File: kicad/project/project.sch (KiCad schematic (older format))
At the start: 47 parts, among them J1 SWD, J3 Voltmeter, Q1 Si2319CDS, Q2 2N7002, U1 ADS1015, U2 AP7380, U3 STM32L031F4Px, U4 VN7003ALH

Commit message: Tuning
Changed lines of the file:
@@
 	1400 7275 1400 7125
-Wire Wire Line
-	4300 3925 4550 3925
 Wire Wire Line
 	6000 3075 6000 3150
@@
 	0    -1   -1   0
 $EndComp
-Connection ~ 4550 3925
-Wire Wire Line
-	4550 3925 6650 3925
 Wire Wire Line
 	6850 4225 6850 4075
@@
 	9925 2975 9825 2975
 Connection ~ 9825 2975
+Wire Wire Line
+	4550 3925 6650 3925
 $EndSCHEMATC

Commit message: VN7004CLHTR
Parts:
- removed BT1: Battery_Meter, theapi:TerminalBlock_Meter, symbol theapi_Battery:Battery_Meter
- removed C2: 0.1UF, Capacitor_SMD:C_0603_1608Metric_Pad1.05x0.95mm_HandSolder, symbol project-rescue:C-stm32l053c-rescue
- removed D5: D_Schottky, Diode_THT:D_DO-201AD_P12.70mm_Horizontal, symbol Device:D_Schottky
- removed H3, H4: MountingHole_Pad, MountingHole:MountingHole_3.2mm_M3_Pad, symbol Mechanical:MountingHole_Pad
- removed J3: Voltmeter, theapi:Voltmeter_Header_1x03, symbol Connector:Conn_01x03_Male
- removed R4, R5, R6: 10K, Resistor_SMD:R_0603_1608Metric_Pad1.05x0.95mm_HandSolder, symbol project-rescue:R-stm32l053c-rescue
- removed TP1: TestPoint, TestPoint:TestPoint_Pad_D1.0mm, symbol Connector:TestPoint
- removed U1: ADS1015, theapi:TSSOP-10_3x3mm_P0.5mm, symbol project-rescue:ADS1015-adc
- added BT1: Battery, TerminalBlock:TerminalBlock_bornier-2_P5.08mm, symbol Device:Battery
- C9: value 1uF -> 220pF
- U4: value VN7003ALH -> VN7004CLHTR
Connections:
- net GND: now also BT1.2 (-)
- net OUT: now also Q1.2 (S), BT1.1 (+)
- net at Q1.3 (D), R14.1: now also R10.1
- net at Q1.1 (G), Q2.3 (D): now also R10.2; no longer R10.1
- removed net DIODE: Q1.2 (S), R10.2
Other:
- note removed: "Optional External ADC"
- moved on the sheet: R10

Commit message: VN7004CLHTR
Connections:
- net ADC_RDY: no longer names the net of U3.13 (PA7)
- net SCL: no longer names the net of U3.17 (PA9)
- net SDA: no longer names the net of U3.18 (PA10)
- no-connect marks 1 -> 4
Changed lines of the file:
@@
 	1    0    0    -1
 $EndComp
-Text GLabel 4550 4625 2    50   Input ~ 0
-SCL
-Text GLabel 4550 4725 2    50   Input ~ 0
-SDA
 Text GLabel 3550 4925 0    50   Input ~ 0
 CURRENT_SENSE
@@
 Text GLabel 6150 1850 2    50   Input ~ 0
 UART_TX
-Text GLabel 4550 4525 2    60   Input ~ 0
-ADC_RDY
 Wire Wire Line
 	6000 3075 6000 3150
@@
 Wire Wire Line
 	10225 2675 10225 4475
+NoConn ~ 4550 4625
+NoConn ~ 4550 4525
+NoConn ~ 4550 4725
 $EndSCHEMATC

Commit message: New layout
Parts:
- removed D4: LED, LED_SMD:LED_0805_2012Metric_Pad1.15x1.40mm_HandSolder, symbol Device:LED
- removed H2: MountingHole_Pad, MountingHole:MountingHole_3.2mm_M3_Pad, symbol Mechanical:MountingHole_Pad
- removed R17: 10K, Resistor_SMD:R_0603_1608Metric_Pad1.05x0.95mm_HandSolder, symbol Device:R
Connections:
- net OUT: now also R10.1
- net at Q1.3 (D), R14.1: no longer R10.1
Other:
- moved on the sheet: R10
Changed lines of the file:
@@
 	8625 3500 9125 3500
-$Comp
-L Device:R R17
-U 1 1 5C7C0432
-P 9150 4850
-F 0 "R17" H 9220 4896 50  0000 L CNN
-F 1 "10K" H 9220 4805 50  0000 L CNN
-F 2 "Resistor_SMD:R_0603_1608Metric_Pad1.05x0.95mm_HandSolder" V 9080 4850 50  0001 C CNN
-F 3 "~" H 9150 4850 50  0001 C CNN
-	1    9150 4850
-	1    0    0    -1
-$EndComp
-$Comp
-L Device:LED D4
-U 1 1 5C7C051B
-P 9150 5300
-F 0 "D4" V 9188 5183 50  0000 R CNN
-F 1 "LED" V 9097 5183 50  0000 R CNN
-F 2 "LED_SMD:LED_0805_2012Metric_Pad1.15x1.40mm_HandSolder" H 9150 5300 50  0001 C CNN
-F 3 "~" H 9150 5300 50  0001 C CNN
-	1    9150 5300
-	0    -1   -1   0
-$EndComp
-$Comp
-L power:GND #PWR032
-U 1 1 5C7C05D8
-P 9150 5450
-F 0 "#PWR032" H 9150 5200 50  0001 C CNN
-F 1 "GND" H 9155 5277 50  0000 C CNN
-F 2 "" H 9150 5450 50  0001 C CNN
-F 3 "" H 9150 5450 50  0001 C CNN
-	1    9150 5450
-	1    0    0    -1
-$EndComp
-Wire Wire Line
-	9150 5150 9150 5000
 $Comp
 L Device:LED D1
@@
 	8900 4675 8900 4575
 Connection ~ 8900 4575
-Wire Wire Line
-	8900 4475 9150 4475
 Connection ~ 8900 4475
-Wire Wire Line
-	9150 4700 9150 4475
-Connection ~ 9150 4475
 NoConn ~ 4550 4125
 Text Label 9325 4475 0    50   ~ 0
@@
 Text Label 5025 4225 0    50   ~ 0
 PA4
-Text Label 9150 5100 0    50   ~ 0
-LED_4
 Wire Wire Line
 	7300 4325 7950 4325
@@
 $EndComp
 $Comp
-L Mechanical:MountingHole_Pad H2
-U 1 1 5C8B1717
-P 10025 1050
-F 0 "H2" H 10125 1101 50  0000 L CNN
-F 1 "MountingHole_Pad" H 10125 1010 50  0000 L CNN
-F 2 "MountingHole:MountingHole_3.2mm_M3_Pad" H 10025 1050 50  0001 C CNN
-F 3 "~" H 10025 1050 50  0001 C CNN
-	1    10025 1050
-	1    0    0    -1
-$EndComp
-$Comp
 L power:GND #PWR034
 U 1 1 5C8BA2A9
@@
 F 3 "" H 9000 1150 50  0001 C CNN
 	1    9000 1150
-	1    0    0    -1
-$EndComp
-$Comp
-L power:GND #PWR037
-U 1 1 5C8BA36C
-P 10025 1150
-F 0 "#PWR037" H 10025 900 50  0001 C CNN
-F 1 "GND" H 10030 977 50  0000 C CNN
-F 2 "" H 10025 1150 50  0001 C CNN
-F 3 "" H 10025 1150 50  0001 C CNN
-	1    10025 1150
 	1    0    0    -1
 $EndComp
@@
 L Device:R R10
 U 1 1 5CB53F25
-P 9475 2825
-F 0 "R10" V 9550 2825 50  0000 C CNN
-F 1 "10K" V 9475 2825 50  0000 C CNN
-F 2 "Resistor_SMD:R_0603_1608Metric_Pad1.05x0.95mm_HandSolder" V 9405 2825 50  0001 C CNN
-F 3 "~" H 9475 2825 50  0001 C CNN
-	1    9475 2825
+P 10100 2825
+F 0 "R10" V 10175 2825 50  0000 C CNN
+F 1 "10K" V 10100 2825 50  0000 C CNN
+F 2 "Resistor_SMD:R_0603_1608Metric_Pad1.05x0.95mm_HandSolder" V 10030 2825 50  0001 C CNN
+F 3 "~" H 10100 2825 50  0001 C CNN
+	1    10100 2825
 	1    0    0    -1
 $EndComp
@@
 	9825 2975 9825 3050
 Wire Wire Line
-	10025 2675 10225 2675
+	10025 2675 10100 2675
 Wire Wire Line
 	9225 3250 8675 3250
@@
 Wire Wire Line
 	8675 2950 7825 2950
-Wire Wire Line
-	7350 2675 9475 2675
 Connection ~ 9825 2975
 Wire Wire Line
@@
 Connection ~ 10225 4475
 Wire Wire Line
-	9150 4475 10225 4475
-Connection ~ 9475 2675
-Wire Wire Line
-	9475 2675 9625 2675
-Wire Wire Line
-	9475 2975 9825 2975
-Wire Wire Line
 	10225 2675 10225 4475
 NoConn ~ 4550 4625
 NoConn ~ 4550 4525
 NoConn ~ 4550 4725
+Connection ~ 10100 2675
+Wire Wire Line
+	10100 2675 10225 2675
+Wire Wire Line
+	9825 2975 10100 2975
+Wire Wire Line
+	7350 2675 9625 2675
+Wire Wire Line
+	8900 4475 10225 4475
 $EndSCHEMATC

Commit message: New layout
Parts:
- removed H1: MountingHole_Pad, MountingHole:MountingHole_3.2mm_M3_Pad, symbol Mechanical:MountingHole_Pad
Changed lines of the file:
@@
 Wire Wire Line
 	7300 4325 7950 4325
-$Comp
-L Mechanical:MountingHole_Pad H1
-U 1 1 5C8B15A7
-P 9000 1050
-F 0 "H1" H 9100 1101 50  0000 L CNN
-F 1 "MountingHole_Pad" H 9100 1010 50  0000 L CNN
-F 2 "MountingHole:MountingHole_3.2mm_M3_Pad" H 9000 1050 50  0001 C CNN
-F 3 "~" H 9000 1050 50  0001 C CNN
-	1    9000 1050
-	1    0    0    -1
-$EndComp
-$Comp
-L power:GND #PWR034
-U 1 1 5C8BA2A9
-P 9000 1150
-F 0 "#PWR034" H 9000 900 50  0001 C CNN
-F 1 "GND" H 9005 977 50  0000 C CNN
-F 2 "" H 9000 1150 50  0001 C CNN
-F 3 "" H 9000 1150 50  0001 C CNN
-	1    9000 1150
-	1    0    0    -1
-$EndComp
 Wire Wire Line
 	6650 3925 6650 3575

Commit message: power
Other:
- moved on the sheet: R10
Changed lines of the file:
@@
 L Device:R R10
 U 1 1 5CB53F25
-P 10100 2825
-F 0 "R10" V 10175 2825 50  0000 C CNN
-F 1 "10K" V 10100 2825 50  0000 C CNN
-F 2 "Resistor_SMD:R_0603_1608Metric_Pad1.05x0.95mm_HandSolder" V 10030 2825 50  0001 C CNN
-F 3 "~" H 10100 2825 50  0001 C CNN
-	1    10100 2825
-	1    0    0    -1
+P 10350 2975
+F 0 "R10" V 10425 2975 50  0000 C CNN
+F 1 "10K" V 10350 2975 50  0000 C CNN
+F 2 "Resistor_SMD:R_0603_1608Metric_Pad1.05x0.95mm_HandSolder" V 10280 2975 50  0001 C CNN
+F 3 "~" H 10350 2975 50  0001 C CNN
+	1    10350 2975
+	0    1    1    0
 $EndComp
 $Comp
@@
 Wire Wire Line
 	9825 2975 9825 3050
-Wire Wire Line
-	10025 2675 10100 2675
 Wire Wire Line
 	9225 3250 8675 3250
@@
 	1    0    0    -1
 $EndComp
+Connection ~ 10500 4475
 Wire Wire Line
-	10500 4475 10225 4475
-Connection ~ 10225 4475
-Wire Wire Line
-	10225 2675 10225 4475
+	10500 2675 10500 2975
 NoConn ~ 4550 4625
 NoConn ~ 4550 4525
 NoConn ~ 4550 4725
-Connection ~ 10100 2675
-Wire Wire Line
-	10100 2675 10225 2675
-Wire Wire Line
-	9825 2975 10100 2975
 Wire Wire Line
 	7350 2675 9625 2675
 Wire Wire Line
-	8900 4475 10225 4475
+	8900 4475 10500 4475
+Connection ~ 10500 2975
+Wire Wire Line
+	10500 2975 10500 4475
+Wire Wire Line
+	10025 2675 10500 2675
+Wire Wire Line
+	9825 2975 10200 2975
 $EndSCHEMATC

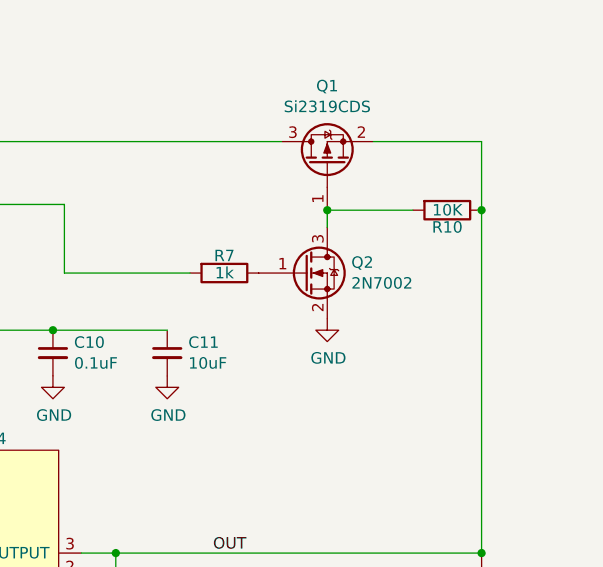
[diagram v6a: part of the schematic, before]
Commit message: mosfet change
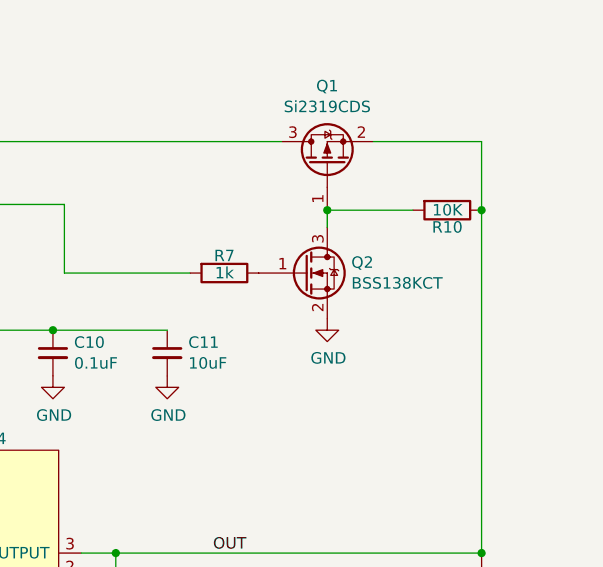
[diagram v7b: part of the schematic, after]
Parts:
- Q2: value 2N7002 -> BSS138KCT
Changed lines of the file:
@@
 P 9725 3250
 F 0 "Q2" H 9930 3296 50  0000 L CNN
-F 1 "2N7002" H 9930 3205 50  0000 L CNN
+F 1 "BSS138KCT" H 9930 3205 50  0000 L CNN
 F 2 "Package_TO_SOT_SMD:SOT-23" H 9925 3175 50  0001 L CIN
 F 3 "https://www.fairchildsemi.com/datasheets/2N/2N7002.pdf" H 9725 3250 50  0001 L CNN

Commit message: Silkscreen
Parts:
- BT1, SC1: footprint TerminalBlock:TerminalBlock_bornier-2_P5.08mm -> theapi:TerminalBlock_2_P5.08mm
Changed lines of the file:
@@
 F 0 "SC1" H 1133 1496 50  0000 L CNN
 F 1 "Solar_Panel" H 1133 1405 50  0000 L CNN
-F 2 "TerminalBlock:TerminalBlock_bornier-2_P5.08mm" V 1025 1510 50  0001 C CNN
+F 2 "theapi:TerminalBlock_2_P5.08mm" V 1025 1510 50  0001 C CNN
 F 3 "~" V 1025 1510 50  0001 C CNN
 	1    1025 1450
@@
 F 0 "BT1" H 10608 4721 50  0000 L CNN
 F 1 "Battery" H 10608 4630 50  0000 L CNN
-F 2 "TerminalBlock:TerminalBlock_bornier-2_P5.08mm" V 10500 4735 50  0001 C CNN
+F 2 "theapi:TerminalBlock_2_P5.08mm" V 10500 4735 50  0001 C CNN
 F 3 "~" V 10500 4735 50  0001 C CNN
 	1    10500 4675
